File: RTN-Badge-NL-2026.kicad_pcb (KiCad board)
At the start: 2 copper layers, 85.5 x 54 mm, 151 parts, among them J1 USB_A_Edge_Connector, J2 DEBUG, J3 GPIO, SW1 BOOT, SW2 RST, SW3 USER1, SW4 USER2, U1 CH32V203F6P6, U2 XC6206PxxxMR, Y1 8MHz

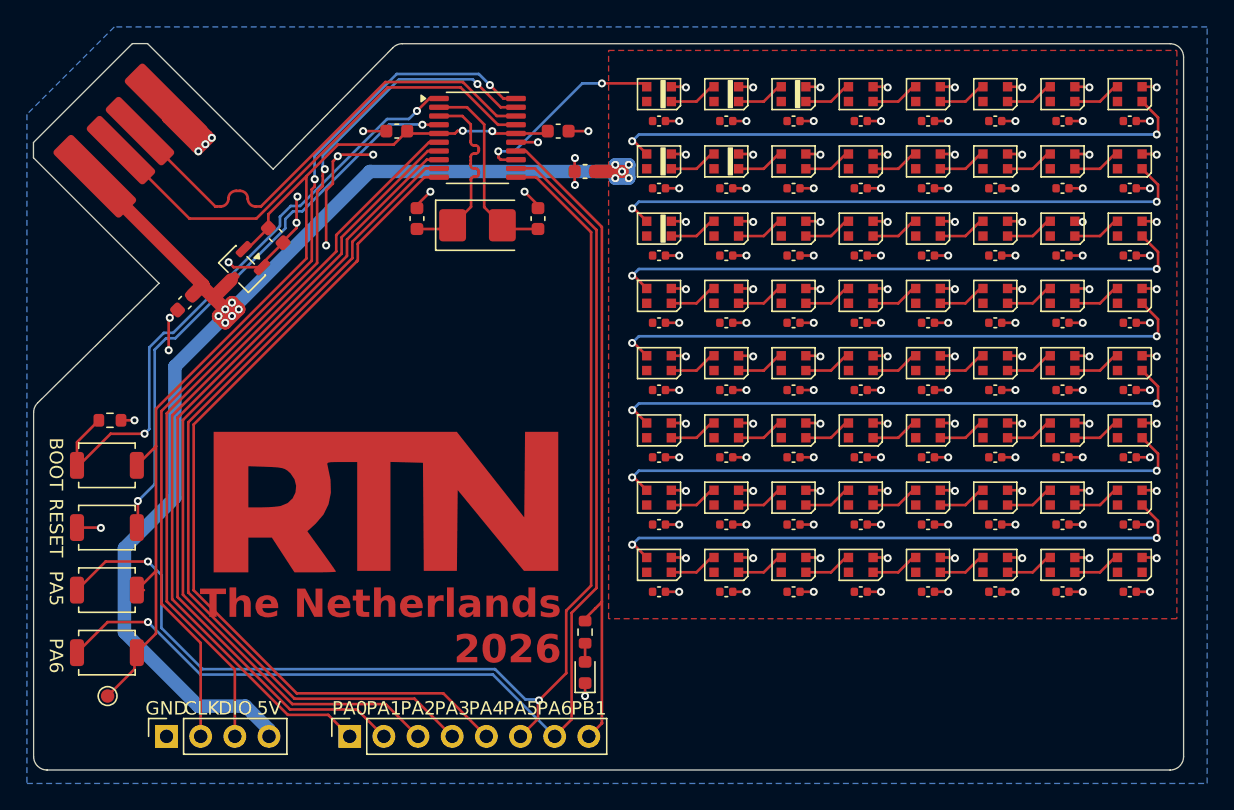
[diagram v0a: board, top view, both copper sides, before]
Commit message: Remove unneeded capacitors from LED matrix
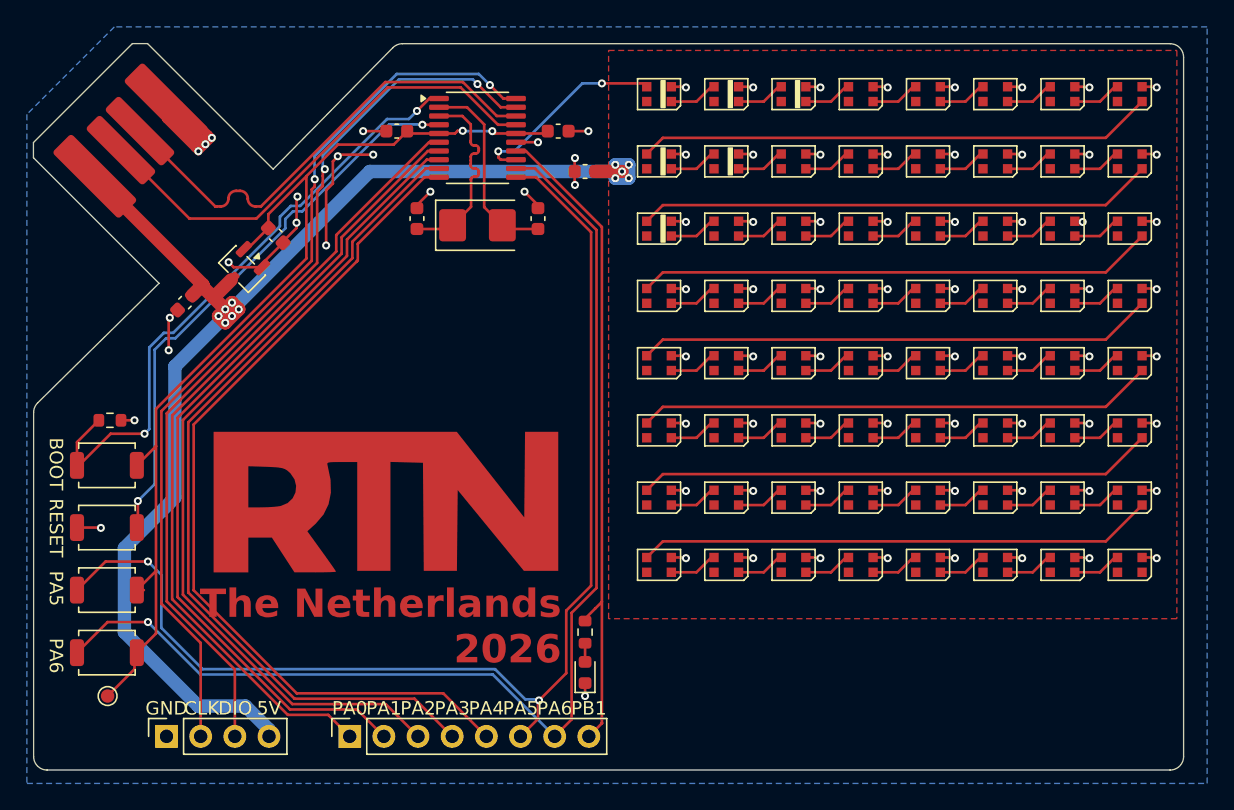
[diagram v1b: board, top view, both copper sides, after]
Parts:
- removed C15, C16, C17, C18, C19, C20, C21, C22, C23, C24, C25, C26, C27, C28, C29, C30, C31, C32, C33, C34, C35, C36, C37, C38, C39, C40, C41, C42, C43, C44, C45, C46, C47, C48, C49, C50, C51, C52, C53, C54, C55, C56, C57, C58, C59, C60, C61, C62, C63, C64, C65, C66, C67, C68, C69, C70, C71, C72, C73, C74, C75, C76, C77, C78: 100nF, Capacitor_SMD:C_0402_1005Metric
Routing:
- net GND: track 194.3 -> 129.0 mm, vias 149 -> 85
- net Net-(D8-DOUT): track 43.7 -> 38.4 mm, vias 2 -> 0
- net Net-(D56-DOUT): track 43.7 -> 38.4 mm, vias 2 -> 0
- net Net-(D40-DOUT): track 43.7 -> 38.4 mm, vias 2 -> 0
- net Net-(D32-DOUT): track 43.7 -> 38.4 mm, vias 2 -> 0
- net Net-(D16-DOUT): track 43.7 -> 38.4 mm, vias 2 -> 0
- net /Matrix/MATRIX_4: track 43.7 -> 38.4 mm, vias 2 -> 0
- net /Matrix/MATRIX_2: track 43.7 -> 38.4 mm, vias 2 -> 0

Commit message: Slightly nudge LED placement, move 3V3 TP and give label
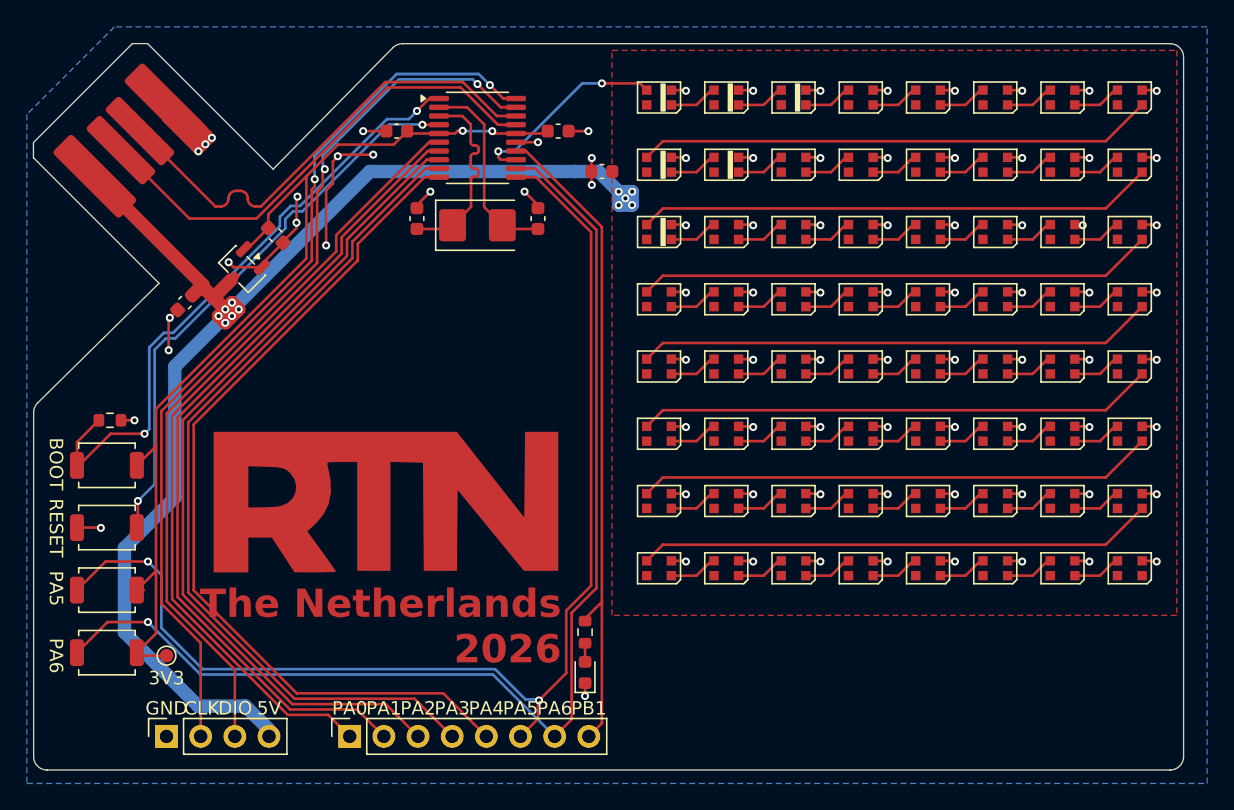
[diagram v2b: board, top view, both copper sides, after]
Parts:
- moved TP1 5.31 mm to (34.9, 70.5)
- moved C2 1.25 mm to (67.2, 34.5)
- moved D1 0.25 mm to (71.5, 29.0)
- moved D10 0.25 mm to (76.5, 34.0)
- moved D11 0.25 mm to (81.5, 34.0)
- moved D12 0.25 mm to (86.5, 34.0)
- moved D13 0.25 mm to (91.5, 34.0)
- moved D14 0.25 mm to (96.5, 34.0)
- moved D15 0.25 mm to (101.5, 34.0)
- moved D16 0.25 mm to (106.5, 34.0)
- moved D17 0.25 mm to (71.5, 39.0)
- moved D18 0.25 mm to (76.5, 39.0)
- moved D19 0.25 mm to (81.5, 39.0)
- moved D2 0.25 mm to (76.5, 29.0)
- moved D20 0.25 mm to (86.5, 39.0)
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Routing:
- net +3V3: track 75.8 -> 74.9 mm
- net +5V: track 101.9 -> 101.0 mm
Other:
- board text added: "3V3"

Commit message: Add grounded mounting holes
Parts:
- added H1: MountingHole_Pad, MountingHole:MountingHole_2.2mm_M2_Pad_Via, F.Cu at (29.0, 75.0)
- added H2: MountingHole_Pad, MountingHole:MountingHole_2.2mm_M2_Pad_Via, F.Cu at (106.5, 75.0)
- added H3: MountingHole_Pad, MountingHole:MountingHole_2.2mm_M2_Pad_Via, F.Cu at (64.5, 28.0)
- moved TP1 1.50 mm to (34.9, 69.0)
- moved SW4 1.35 mm to (30.4, 68.9)
- moved SW1 1.35 mm to (30.4, 55.0)
- moved SW2 1.35 mm to (30.4, 59.6)
- moved SW3 1.35 mm to (30.4, 64.3)
- moved R1 1.00 mm to (30.7, 52.0)
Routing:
- net +3V3: track 74.9 -> 70.9 mm
- net /BOOT: track 46.5 -> 43.0 mm
- net MATRIX_SPI: track 15.2 -> 17.0 mm
- net /RST: track 42.5 -> 41.2 mm
- net /PA6: track 86.8 -> 87.7 mm

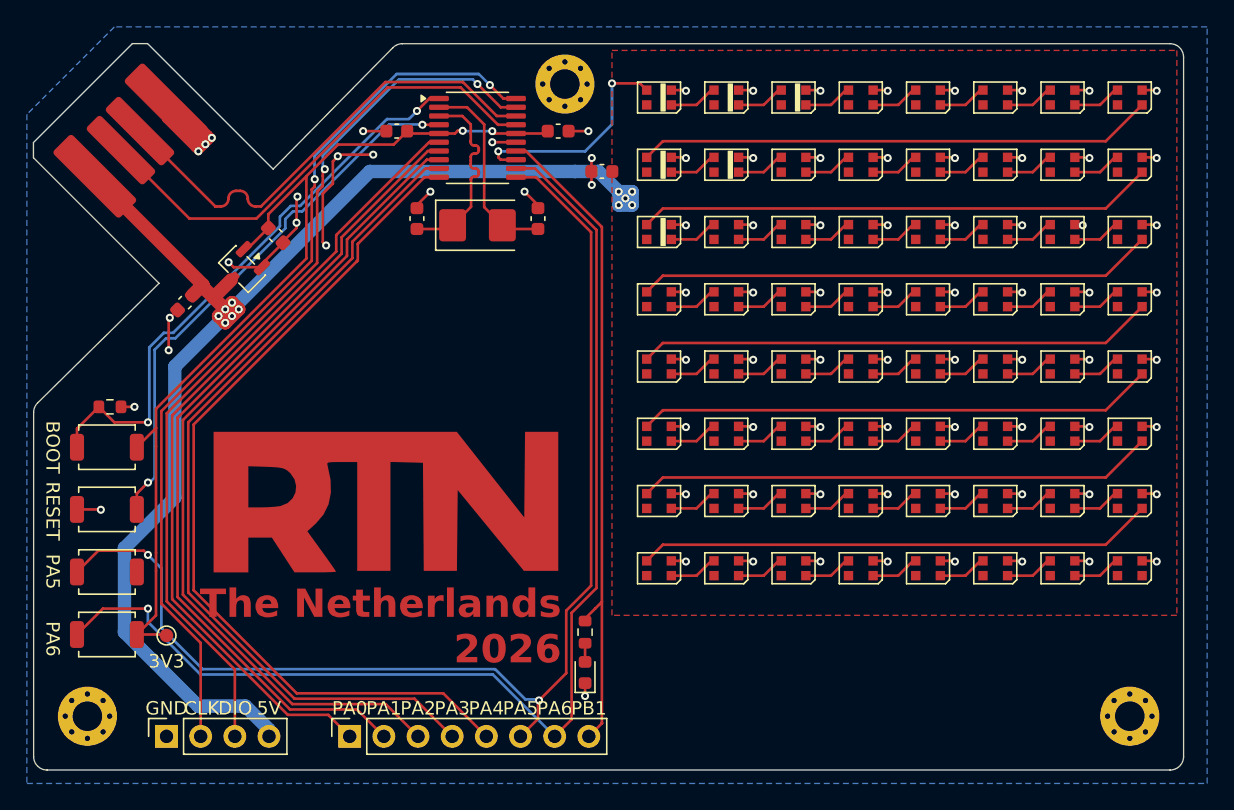
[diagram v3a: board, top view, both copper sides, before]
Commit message: Move debug headers over so they line up with the gpio breakout
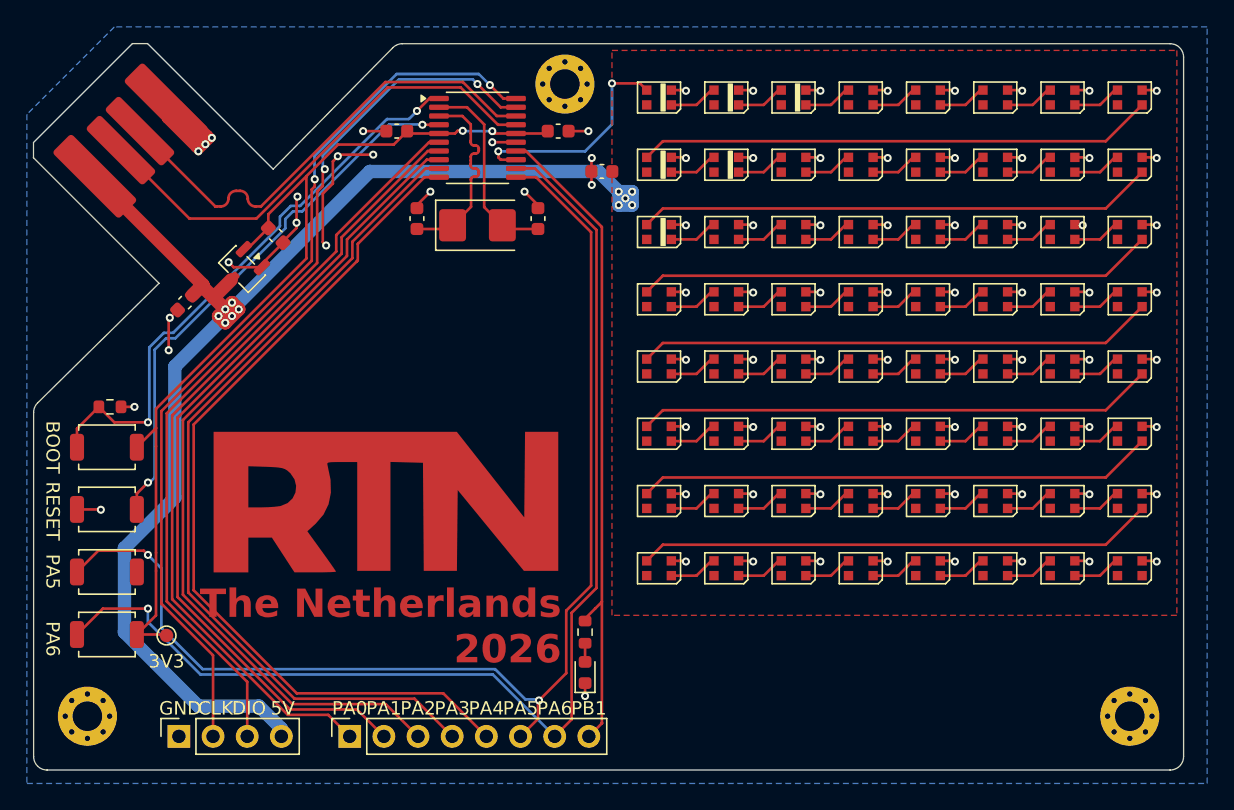
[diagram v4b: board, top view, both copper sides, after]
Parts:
- moved J2 0.92 mm to (35.8, 76.5)
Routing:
- net +5V: track 101.0 -> 102.0 mm

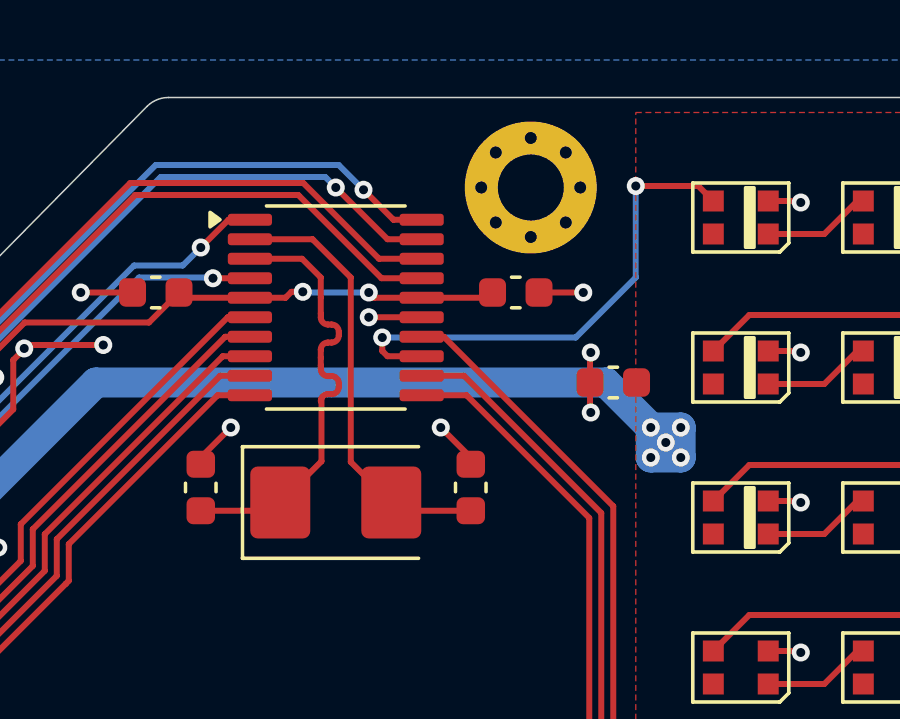
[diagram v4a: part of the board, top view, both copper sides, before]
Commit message: Adjust some traces for aesthetics
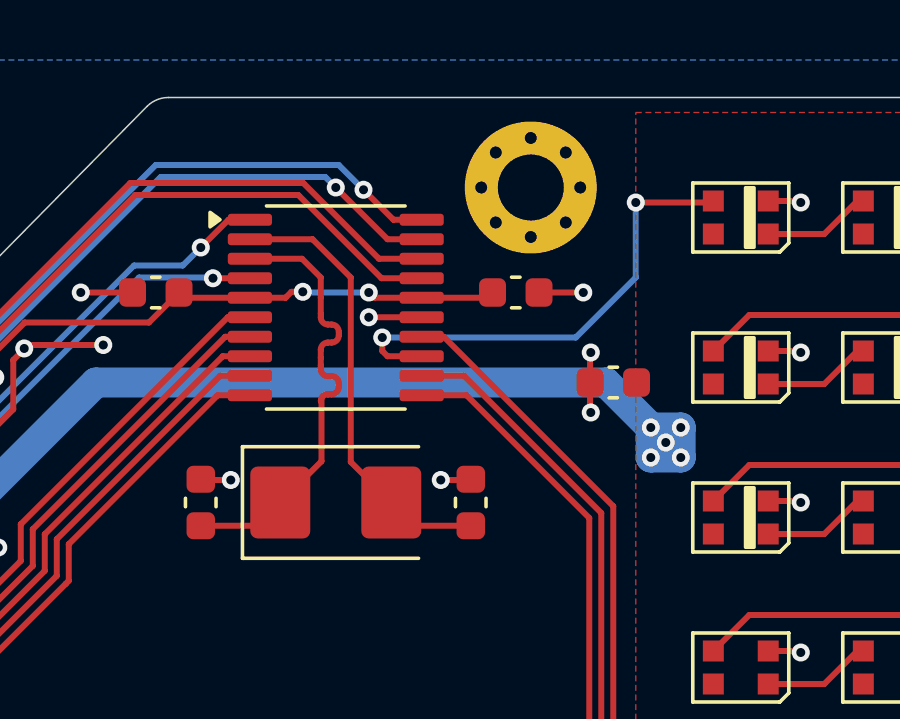
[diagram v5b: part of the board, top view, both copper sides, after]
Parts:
- moved C5 0.50 mm to (62.5, 38.5)
- moved C6 0.50 mm to (53.5, 38.5)
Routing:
- net GND: track 129.2 -> 128.0 mm
- net MATRIX_SPI: track 17.0 -> 16.2 mm
- net Net-(U1-OSC_IN): track 14.3 -> 14.9 mm
- net Net-(U1-OSC_OUT): track 14.7 -> 15.3 mm
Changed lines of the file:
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@@
 	(footprint "Capacitor_SMD:C_0603_1608Metric"
 		(layer "F.Cu")
-		(at 53.5 38 -90)
+		(at 53.5 38.5 -90)
 		(descr "Capacitor SMD 0603 (1608 Metric), square (rectangular) end terminal, IPC-7351 nominal, (Body size source: IPC-SM-782 page 76, https://www.pcb-3d.com/wordpress/wp-content/uploads/ipc-sm-782a_amendment_1_and_2.pdf)")
 		(tags "capacitor")
@@
 	(footprint "Capacitor_SMD:C_0603_1608Metric"
 		(layer "F.Cu")
-		(at 62.5 38 -90)
+		(at 62.5 38.5 -90)
 		(descr "Capacitor SMD 0603 (1608 Metric), square (rectangular) end terminal, IPC-7351 nominal, (Body size source: IPC-SM-782 page 76, https://www.pcb-3d.com/wordpress/wp-content/uploads/ipc-sm-782a_amendment_1_and_2.pdf)")
 		(tags "capacitor")
@@
 	)
 	(segment
+		(start 62.475 37.725)
+		(end 62.5 37.725)
+		(width 0.2)
+		(layer "F.Cu")
+		(net "GND")
+	)
+	(segment
 		(start 73.45 38.45)
 		(end 73.5 38.5)
@@
 	)
 	(segment
-		(start 53.5 37)
-		(end 54.5 36)
-		(width 0.2)
-		(layer "F.Cu")
-		(net "GND")
-	)
-	(segment
 		(start 72.415 48.45)
 		(end 73.45 48.45)
@@
 	)
 	(segment
-		(start 53.5 37.225)
-		(end 53.5 37)
-		(width 0.2)
-		(layer "F.Cu")
-		(net "GND")
-	)
-	(segment
-		(start 62.5 37)
-		(end 61.5 36)
-		(width 0.2)
-		(layer "F.Cu")
-		(net "GND")
-	)
-	(segment
 		(start 35 45.5)
 		(end 35.125 45.375)
@@
 	)
 	(segment
+		(start 61.5 37.75)
+		(end 62.45 37.75)
+		(width 0.2)
+		(layer "F.Cu")
+		(net "GND")
+	)
+	(segment
 		(start 92.415 33.45)
 		(end 93.45 33.45)
@@
 	)
 	(segment
+		(start 62.45 37.75)
+		(end 62.475 37.725)
+		(width 0.2)
+		(layer "F.Cu")
+		(net "GND")
+	)
+	(segment
 		(start 92.415 63.45)
 		(end 93.45 63.45)
@@
 	)
 	(segment
+		(start 53.525 37.725)
+		(end 53.5 37.725)
+		(width 0.2)
+		(layer "F.Cu")
+		(net "GND")
+	)
+	(segment
 		(start 66.475 34.5)
 		(end 66.475 33.525)
@@
 	)
 	(segment
+		(start 54.5 37.75)
+		(end 53.55 37.75)
+		(width 0.2)
+		(layer "F.Cu")
+		(net "GND")
+	)
+	(segment
 		(start 72.415 53.45)
 		(end 73.45 53.45)
@@
 	)
 	(segment
-		(start 62.5 37.225)
-		(end 62.5 37)
-		(width 0.2)
-		(layer "F.Cu")
-		(net "GND")
-	)
-	(segment
 		(start 44.5475 38.307895)
 		(end 44.5475 36.4324)
@@
 	)
 	(segment
+		(start 53.55 37.75)
+		(end 53.525 37.725)
+		(width 0.2)
+		(layer "F.Cu")
+		(net "GND")
+	)
+	(segment
 		(start 83.45 43.45)
 		(end 83.5 43.5)
@@
 	)
 	(via
-		(at 61.5 36)
+		(at 61.5 37.75)
 		(size 0.6)
 		(drill 0.3)
@@
 	)
 	(via
-		(at 54.5 36)
+		(at 54.5 37.75)
 		(size 0.6)
 		(drill 0.3)
@@
 	)
 	(segment
-		(start 70.085 27.95)
-		(end 70.585 28.45)
+		(start 68 28.5)
+		(end 70.535 28.5)
 		(width 0.2)
 		(layer "F.Cu")
@@
 	)
 	(segment
-		(start 59.55 33)
-		(end 59.55 33.45)
+		(start 70.535 28.5)
+		(end 70.585 28.45)
 		(width 0.2)
 		(layer "F.Cu")
@@
 	)
 	(segment
-		(start 68 27.95)
-		(end 70.085 27.95)
+		(start 59.55 33)
+		(end 59.55 33.45)
 		(width 0.2)
 		(layer "F.Cu")
@@
 	)
 	(via
-		(at 68 27.95)
+		(at 68 28.5)
 		(size 0.6)
 		(drill 0.3)
@@
 	)
 	(segment
-		(start 68 31)
-		(end 66 33)
+		(start 66 33)
+		(end 59.55 33)
 		(width 0.2)
 		(layer "B.Cu")
@@
 	)
 	(segment
-		(start 68 27.95)
+		(start 68 28.5)
 		(end 68 31)
 		(width 0.2)
@@
 	)
 	(segment
-		(start 66 33)
-		(end 59.55 33)
+		(start 68 31)
+		(end 66 33)
 		(width 0.2)
 		(layer "B.Cu")
@@
 	)
 	(segment
-		(start 53.5 38.775)
-		(end 55.874999 38.775)
-		(width 0.2)
-		(layer "F.Cu")
-		(net "Net-(U1-OSC_OUT)")
-	)
-	(segment
 		(start 57.5 31.665834)
 		(end 57.5 31)
@@
 	)
 	(segment
+		(start 56.149999 38.5)
+		(end 55.374999 39.275)
+		(width 0.2)
+		(layer "F.Cu")
+		(net "Net-(U1-OSC_OUT)")
+	)
+	(segment
 		(start 58.1 32.927661)
 		(end 58.1 32.807661)
@@
 	)
 	(segment
+		(start 55.374999 39.275)
+		(end 53.5 39.275)
+		(width 0.2)
+		(layer "F.Cu")
+		(net "Net-(U1-OSC_OUT)")
+	)
+	(segment
 		(start 57.523768 37.126231)
 		(end 56.149999 38.5)
@@
 	(segment
 		(start 59.850001 38.5)
+		(end 60.625001 39.275)
+		(width 0.2)
+		(layer "F.Cu")
+		(net "Net-(U1-OSC_IN)")
+	)
+	(segment
+		(start 59.850001 38.5)
 		(end 58.5 37.149999)
 		(width 0.2)
@@
 	)
 	(segment
-		(start 62.5 38.775)
-		(end 60.125001 38.775)
+		(start 60.625001 39.275)
+		(end 62.5 39.275)
 		(width 0.2)
 		(layer "F.Cu")
